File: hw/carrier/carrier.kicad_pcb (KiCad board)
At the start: 2 copper layers, 70 x 50 mm, 50 parts, among them J2 PCM5102A I2S, J3 PCM5102A analog, J4 MAX4466 pigtail, J5 TP4056 OUT-/B-, J6 TP4056 B+/OUT+, J7 debug TX, J8 LiPo JST-PH, J9 TP4056 IN+ wire (J6b), Q1 DMG3415U, Q2 BC557, SW1 power SPDT 1A, SW2 MODE 6x6, U1 TL431, X1 scope X RCA pads, Y1 scope Y RCA pads

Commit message: cad v2
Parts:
- J5: footprint PinSocket_1x02_P2.54mm_Vertical -> TP4056_Pads_OUTminus_Bminus
- J6: footprint PinSocket_1x02_P2.54mm_Vertical -> TP4056_Pads_Bplus_OUTplus
- moved U1 27.0 mm to (6.00, 35.5), turned to 0 degrees
- moved R8 21.9 mm to (15.0, 37.0)
- moved R7 21.8 mm to (15.0, 33.5)
- moved TP4 19.4 mm to (37.5, 28.0)
- moved R9 17.4 mm to (21.0, 33.5)
- moved Q2 16.7 mm to (6.00, 29.5)
- moved C2 16.4 mm to (17.5, 28.5), turned to 0 degrees
- moved JB1 15.2 mm to (20.3, 9.30)
- moved JA1 15.2 mm to (20.3, 24.5)
- moved R12 11.3 mm to (33.0, 33.5)
- moved R6 10.6 mm to (27.0, 33.5)
- moved C5 9.22 mm to (31.5, 25.5), turned to 0 degrees
- moved D3 7.48 mm to (61.0, 23.0)
- moved TP2 7.38 mm to (39.0, 30.0)
- moved J6 5.61 mm to (45.7, 37.4)
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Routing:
- net 3V3: track 321.5 -> 105.1 mm, vias 7 -> 4
- net LED_MODE_A: track 21.1 -> 114.2 mm, vias 0 -> 7
- net VLOAD: track 213.7 -> 147.0 mm, vias 6 -> 5
- net BAT_MINUS: track 62.1 -> 19.9 mm, vias 1 -> 0
- net VSW: track 78.4 -> 113.5 mm, vias 6 -> 2
- net GATE: track 59.8 -> 92.0 mm, vias 1 -> 9
- net VBAT_SENSE: track 25.8 -> 50.1 mm, vias 0 -> 1
- net LED_NET_A: track 19.4 -> 39.7 mm
- net DBG_TX: track 4.70 -> 24.1 mm
- net POT_WIPER: track 59.6 -> 41.0 mm, vias 0 -> 2
- net BAT_PLUS: track 89.8 -> 72.1 mm, vias 2 -> 1
- net BTN_MODE: track 29.1 -> 44.4 mm, vias 1 -> 0
- net Q2_B: track 24.7 -> 33.6 mm, vias 1 -> 2
- net I2S_LRCK: track 17.5 -> 8.68 mm, vias 2 -> 0
- net D5_A: track 6.35 -> 14.2 mm, vias 1 -> 0
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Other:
- board text added: "+ cell -"
- board text added: "B+"
- board text added: "B-"
- board text added: "B- is NOT GND"
- board text added: "ESP32-C3 SuperMini"
- board text added: "GY-PCM5102A"
- board text added: "HYPEROSCI carrier v1.1 2026-07"
- board text added: "HYPEROSCI v1.1"
- board text added: "IN+"
- board text added: "MODE SW"
- board text added: "OUT+"
- board text added: "OUT-"
- board text removed: "+"
- board text removed: "-"
- board text removed: "B- != GND!"
- board text removed: "ESP32-C3"
- board text removed: "HYPEROSCI carrier v1.0 2026-07"
- board text removed: "IN+ (J6b)"
- board text removed: "J1A"
- board text removed: "J1B"
- board text removed: "PCM5102A"
- board text removed: "X"
- board text removed: "Y"

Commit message: hw+docs: apply the 2026-07-26 power-path design review
Multi-agent adversarial review of the carrier's §4 load-sharing power path
(docs/hardware/pcb-review-findings.md, added here) found the TL431 trip
point mis-derived and several safety-critical instructions wrong.  This
applies the fixes and reconciles every document that repeated them.

BOM / netlist (design.py is the source of truth; board + schematic regenerated):
  - R7 75k -> 8.2k, R8 10k, R9 2.2k -> 1k.  The old derivation dropped the
    TL431 REF bias term (I_ref*R7); with 75k it dominated and the divider
    could not reach the trip window at all.  Trip is now ~4.56 V.
  - D1 1N4148 -> BAT85 (Schottky, keeps the gate pulled low enough).
  - U1 TL431 -> TL431A (2% grade; the 1% window needs it).

Safety-critical doc corrections:
  - The JP1 escape hatch must also omit D2 -- bridging JP1 with D2 fitted
    shorts VBUS_CHG to the cell through one Schottky.  It must further omit
    R7/R8, which JP1 ties straight across the cell (231 uA with no
    comparator left to feed).  Recipe now identical in pcb.md §4.4, §4.5
    and design.py's docstring.
  - TO-92 lead-order trap documented at the netlist and in §5: onsemi
    numbers U1/Q2 1=REF,2=A,3=K, TI numbers the same package the other way
    round, and the anode is the centre lead in both -- so a TI-branded part
    drops into the footprint perfectly while sitting backwards.
  - "No USB while the battery switch is ON" is restored as a permanent rule
    until §4.4 passes on an assembled board; the review found the
    SuperMini-side threshold detection unreliable against a sagging port.

Tooling:
  - FP_OVERRIDE (11 vertical resistors) moved from gen_board.py into
    design.py so gen_schematic.py sees the same footprints; --schematic-parity
    had been flagging 11 resistors the schematic thought were horizontal.
  - route.py: new ROUTE_WIDTH_FLOOR env knob (per-net minimum track width).
    Used to measure a 14-variant VLOAD/VSW width sweep; the wider re-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
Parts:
- D1: value 1N4148 -> BAT85
- R7: value 82k 1% -> 8.2k 1%
- R8: value 100k 1% -> 10k 1%
- R9: value 2.2k -> 1k
- U1: value TL431 -> TL431A

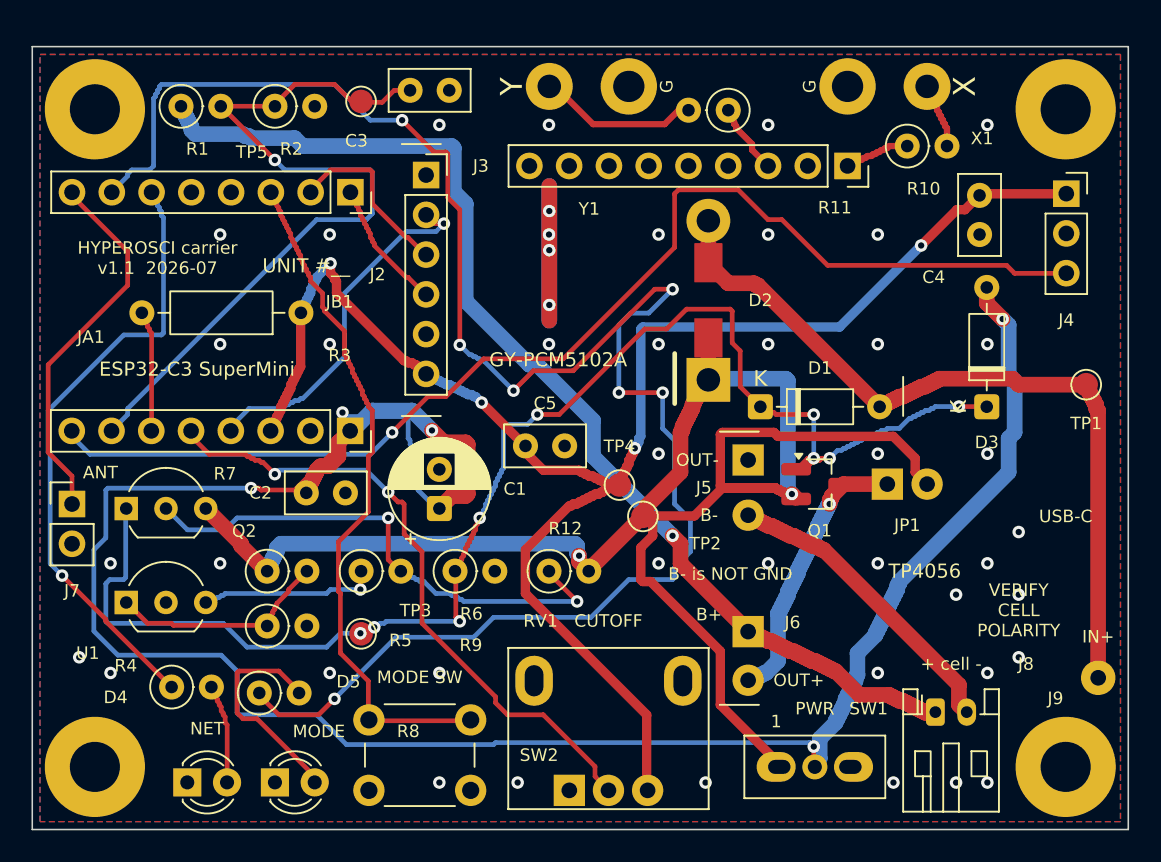
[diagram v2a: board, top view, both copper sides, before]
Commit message: hw/carrier: RV1 was the wrong part's footprint — corrected, re-routed
The RV097NS 5-pin is "mono WITH SWITCH", right-angle.  RV097NS_Vertical
drew it as a vertical pot with two mechanical bracket lugs: row 2 as oval
slots 9.5 mm apart and 7.0 mm behind the pot row, taken "from the common
RV09 drawing" and flagged unverified since the first commit.  The real
part has no bracket lugs at all.  Row 2 is a plain SPST on 1.0 mm holes
5.0 mm apart and 6.25 mm behind, and the mounting surface sits 5.0 mm in
FRONT of the pot row, not 1.2 mm.  Every row-2 pad was 2.25 mm out in X
and 0.75 mm in Y.  The part would not have gone into the board.

Settled by the seller's mechanical drawing, which agrees to the decimal
with KiCad's stock Potentiometer_Alps_RK097_Single_Horizontal_Switch
(from ALPS rk097.pdf) -- and independently by its 9.5 x 11.35 mm
cross-section matching the 2026-07-18 calipers' 9.5 x 11.3.

  - footprint renamed RV097NS_Vertical -> RV097NS_Horizontal_Switch; body
    9.5 x 13.0, bushing and 15 mm shaft on F.Fab, silk open on the
    mounting face because that face lands on Edge.Cuts.
  - RV1's Y stopped being a free parameter: 45.0 puts the mounting
    surface exactly on the board's south edge (y=50), so the M7x0.75
    bushing and shaft hang off it and through the enclosure wall.
  - pads 4/5 stay on GND, deliberately.  No safe spare GPIO exists
    (GPIO0 is MIC_OUT; GPIO8/9 are strapping pins that must be high at
    reset and this switch makes at one end of rotation; GPIO21 is the
    console UART TX, an output), and with no bracket lugs those two
    0.8 mm pins in the pour are the part's only rear anchoring against a
    bare shaft turned by hand.  Symbol says S1/S2 now, not LUG.

Two things broke on the way, both fixed in the generators:

  - ROUTE_SEED 77 stopped working.  Moving five pads was enough: phase D
    ended STUCK with 3 unbridgeable pour clusters and DRC reported 2
    unconnected GND_main islands.  A 24-variant sweep (6 seeds x 4 halo
    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
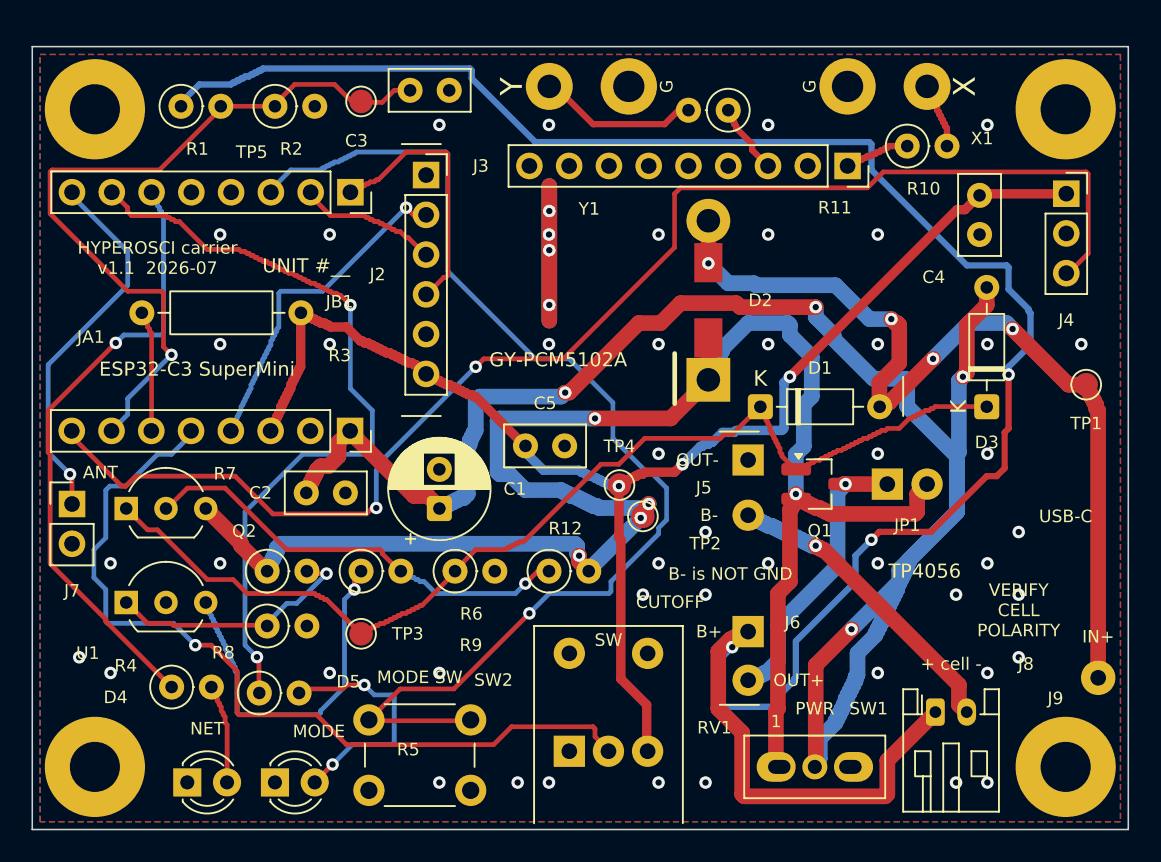
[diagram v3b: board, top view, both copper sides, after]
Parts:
- RV1: value RV097NS B10K -> RV097NS B10K +SW; footprint RV097NS_Vertical -> RV097NS_Horizontal_Switch
- moved RV1 2.50 mm to (36.8, 45.0)
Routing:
- net LED_MODE_A: track 114.2 -> 50.0 mm, vias 7 -> 2
- net BAT_PLUS: track 72.1 -> 134.5 mm, vias 1 -> 3
- net BTN_MODE: track 44.4 -> 74.5 mm, vias 0 -> 1
- net VLOAD: track 147.0 -> 118.9 mm, vias 5 -> 4
- net GATE: track 92.0 -> 68.6 mm, vias 9 -> 0
- net 3V3: track 105.1 -> 88.9 mm, vias 4 -> 3
- net POT_WIPER: track 41.0 -> 54.6 mm, vias 2 -> 1
- net MIC_OUT: track 75.6 -> 87.5 mm, vias 1 -> 2
- net TL431_K: track 11.4 -> 23.3 mm
- net I2S_LRCK: track 8.68 -> 17.0 mm
- net VBUS_CHG: track 50.4 -> 57.9 mm, vias 0 -> 4
- net Q2_B: track 33.6 -> 28.5 mm, vias 2 -> 1
- net I2S_DOUT: track 11.5 -> 9.20 mm
- net VSW_SENSE: track 14.0 -> 16.2 mm, vias 0 -> 1
- net D5_A: track 14.2 -> 15.7 mm, vias 0 -> 2
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
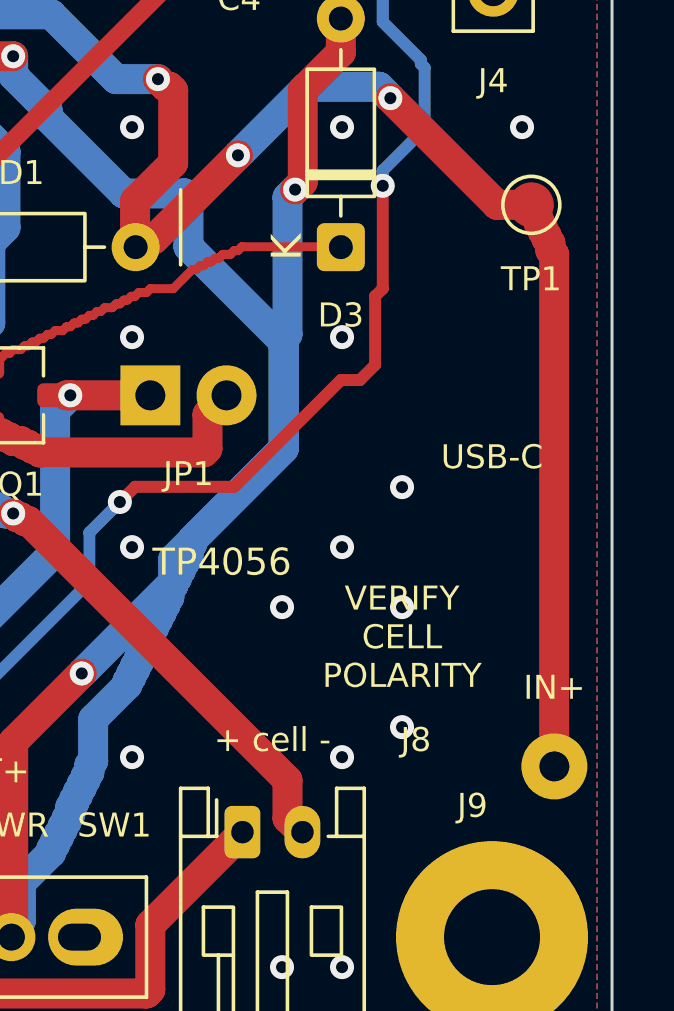
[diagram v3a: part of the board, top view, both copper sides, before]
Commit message: hw/carrier: the TP4056 was a 21.65 mm cantilever — second mount row added
J5/J6 put all four pins in ONE column at one end of the module, and the
USB-C jack is at the other.  A row of pins resists rotation about its own
axis only by bending, so the charge port sat on a diving board:

  0.64 mm square pin, ~5 mm free length -> EI/L = 0.061 N*m/rad each
  four of them, all on the axis         -> ~0.25 N*m/rad total
  5 N off-axis nudge on the plug        -> 0.11 N*m -> ~25 deg

Crude (a machined socket grips several mm of barrel, so reality is
stiffer), but the order of magnitude is the point: grams of side load,
tens of degrees, on the one connector handled every charge cycle at
10-20 N of insertion force.

The module already carried the fix.  Two ~2.8 mm bare-copper pads on
1.68 mm plated holes sit at its USB-C-end corners, in line with OUT+
("+" silk, next to R8) and OUT-.  The carrier already had a pad on one
of them -- J9, drawn as a wire pad for the IN+ sense tap.  So:

  - J9 became a machined socket and moved 0.65 mm west onto the real
    hole.  That also deletes the one hand-soldered wire in the power
    path, which in 4.3 state 2 carries the WHOLE board load (~150 mA
    average, ~350 mA WiFi bursts, ~4 A/<100 us C1 inrush), not a sense
    current.
  - J10 was added on the other corner, ON NO NET.  pcb.md 2 asserts
    TP4056 IN- is the same copper as OUT- and that is the usual
    protected topology, but it has never been ohmed on this module --
    and if it is wrong, bonding it to carrier GND shorts across the
    DW01/FS8205 and the cell loses its protection.  A floating pin
    anchors the far end just as well, so the question stays open.
  - WirePad_D1.0 -> TP4056_MountPin (same 1.0 mm drill / 2.2 mm pad; the
    name and the docstring were the only wrong parts).
  - BOM: six machined single-pin sockets per board, not four.

Why the offset is a caliper number overriding the photogrammetry, which
is the only place in measured.py that happens.  The pi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
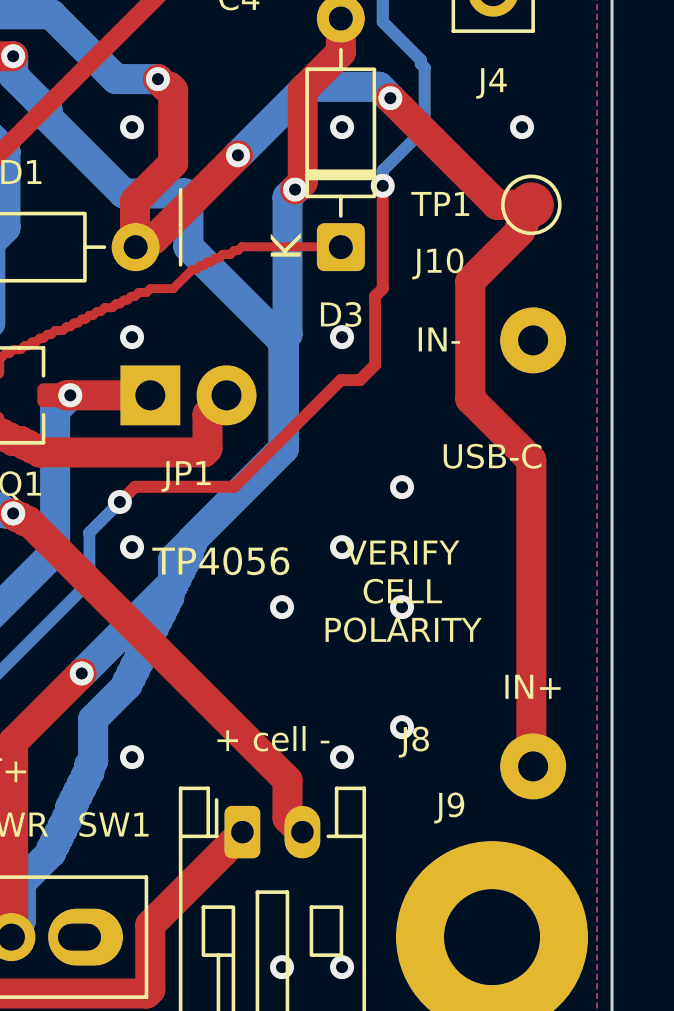
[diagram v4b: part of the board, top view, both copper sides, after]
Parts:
- added J10: TP4056 IN- / mount, TP4056_MountPin, F.Cu at (67.4, 26.1)
- J9: value TP4056 IN+ wire (J6b) -> TP4056 IN+ / mount (J6b); footprint WirePad_D1.0 -> TP4056_MountPin
- moved J9 0.71 mm to (67.4, 40.3)
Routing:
- net VBUS_CHG: track 57.9 -> 59.0 mm
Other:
- board text added: "IN-"
